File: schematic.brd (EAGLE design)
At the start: 52.1 x 134.6 mm, 101 parts, among them IC1 AD8015, IC2 AD8015, IC3 AD8015, IC4 AD8015

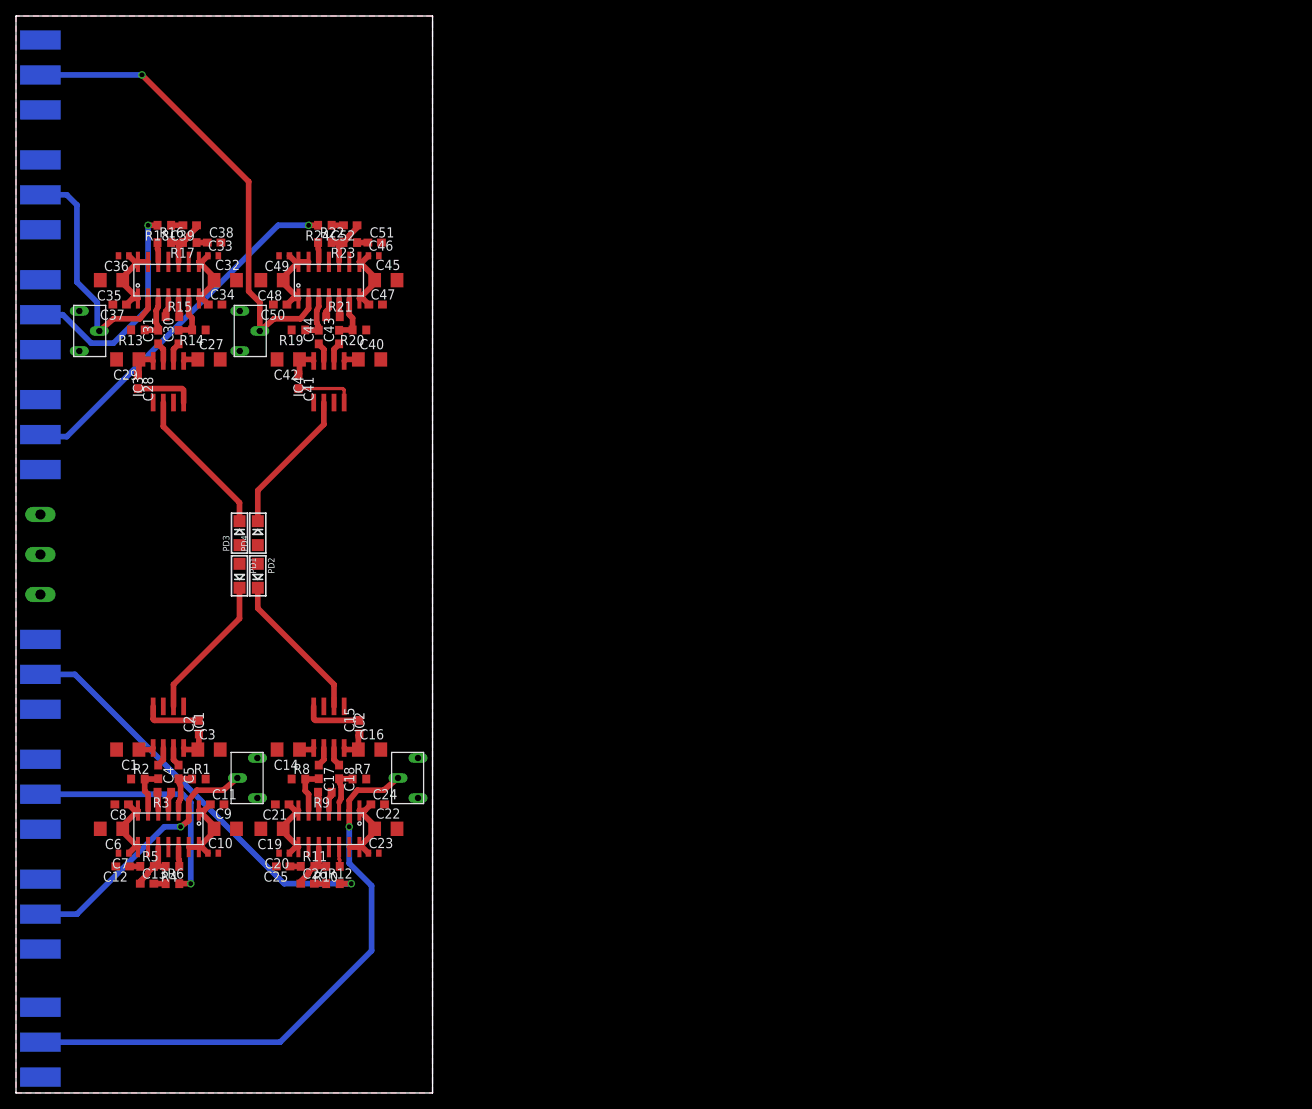
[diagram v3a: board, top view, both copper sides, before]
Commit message: Added LMH6624 to end. Major layout rework for high freq AC .
Still has problems. LMH6624 has power inputs on the wrong side of the
chip making it hard to wire to power plane. GND plane is heavily split
in the process of connecting power planes.
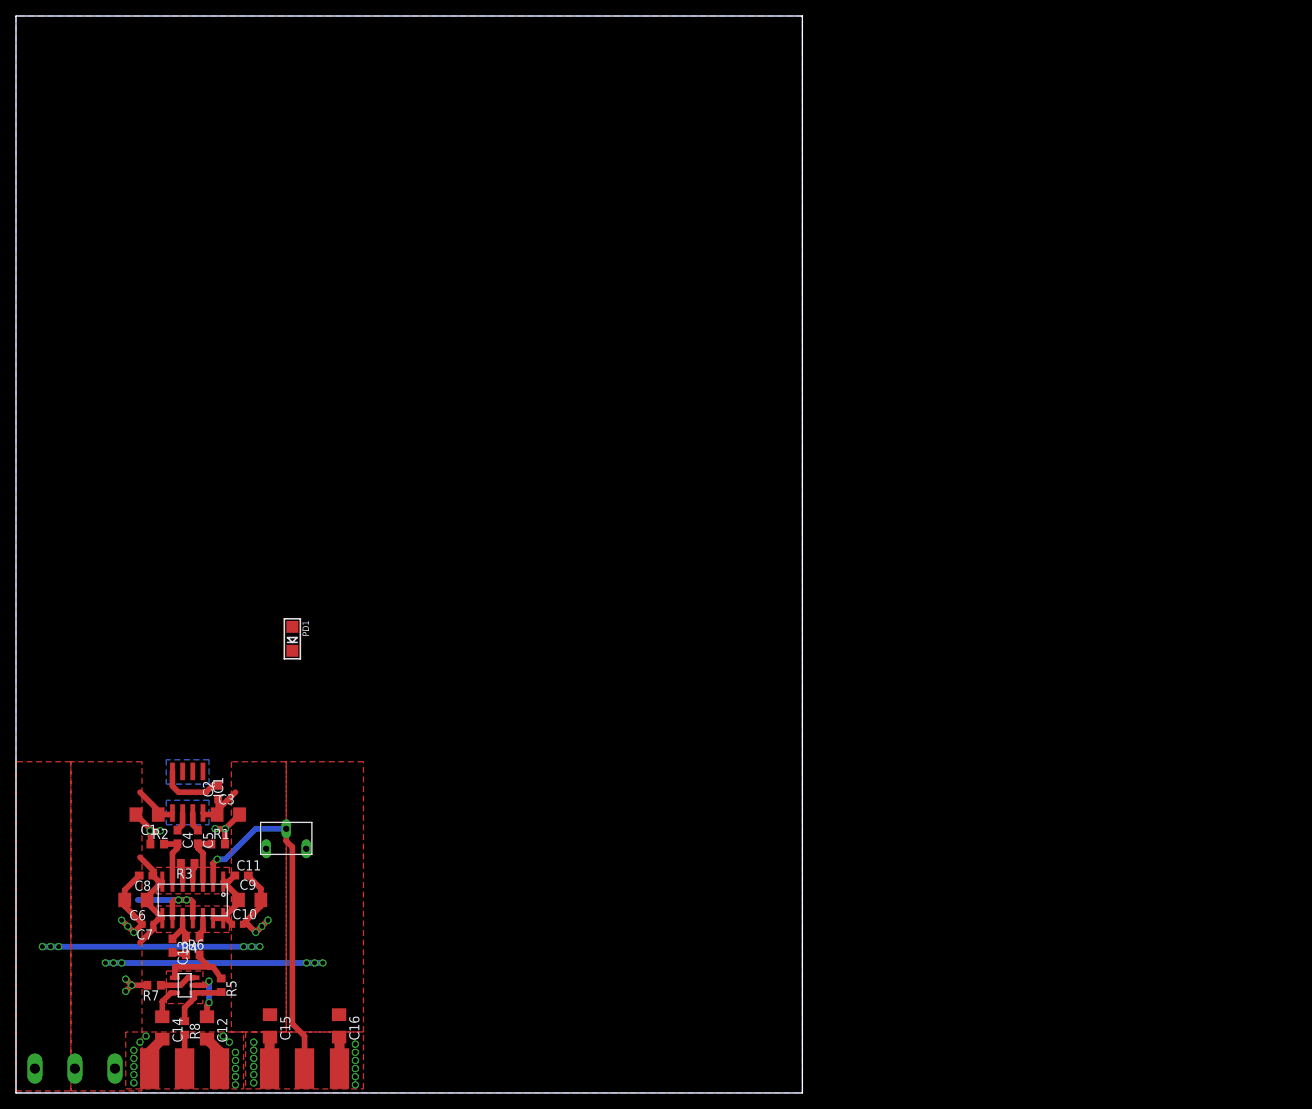
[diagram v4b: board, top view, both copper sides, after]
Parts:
- removed C17, C18, C28, C30, C31, C41, C43, C44: .1uF, rcl:C0603
- removed C19, C22, C27, C29, C32, C35, C40, C42, C45, C48: 6.8uF, rcl:C1206
- removed C20, C23, C33, C36, C46, C49: 0.1uF, rcl:C0402
- removed C21, C24, C26, C34, C37, C39, C47, C50, C52: 0.1uF, rcl:C0603
- removed C25, C38, C51: 39pF, rcl:C0603
- removed IC2, IC3, IC4: AD8015, analog-devices:SO8
- removed PD2, PD3, PD4: (no value), microbuilder:CHIPLED_1206
- removed R10, R16, R22: 1k, rcl:R0603
- removed R11, R12, R15, R17, R18, R21, R23, R24, R9: 100, rcl:R0603
- removed R13, R14, R19, R20: 50, rcl:R0603
- removed U$10, U$14: LMH6503, 12-ChannelEMG:SOIC14
- removed U$11, U$15, U$7: PV37W, 12-ChannelEMG:PV37W
- removed U$12, U$13, U$16, U$17, U$8, U$9: BNCCONN, 12-ChannelEMG:BNCPADS
- C12: value 39pF -> 6.8uF; device rcl:C0603 -> rcl:C1206
- C13: value 0.1uF -> 2.2uF
- C15: value .1uF -> 6.8uF; device rcl:C0603 -> rcl:C1206
- C4, C5: value .1uF -> 2.2uF
- R5: value 100 -> 500
- R6: value 100 -> 30
- R7: value 50 -> 28
- U$6: value LMH6503 -> LMH6624; device 12-ChannelEMG:SOIC14 -> 12-ChannelEMG:SOT-23
- moved U$3 64.4 mm to (7.37, 3.05), turned to 180 degrees
- moved C15 39.0 mm to (31.8, 8.38), turned to 270 degrees
- moved U$5 38.7 mm to (21.1, 3.05), flipped to the top, turned to 0 degrees
- moved U$4 38.2 mm to (36.1, 3.05), flipped to the top, turned to 0 degrees
- moved C14 38.2 mm to (18.3, 8.13), turned to 270 degrees
- moved R7 36.4 mm to (17.3, 13.5), turned to 180 degrees
- moved C16 34.8 mm to (40.4, 8.38), turned to 270 degrees
- moved R8 34.2 mm to (21.1, 8.13), turned to 270 degrees
- moved U$6 26.6 mm to (21.1, 13.5), turned to 90 degrees
- moved C12 22.8 mm to (23.9, 8.13), turned to 270 degrees
- moved R5 17.5 mm to (25.7, 13.5), turned to 270 degrees
- moved PD1 10.3 mm to (34.5, 56.8)
- moved C6 9.40 mm to (15.0, 24.1)
- moved C9 9.40 mm to (29.2, 24.1)
- moved U$1 9.40 mm to (22.1, 24.1)
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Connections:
- removed net N$17: C18.1, IC2.7
- removed net N$18: C17.1, IC2.6
- removed net N$19: C17.2, R8.2, U$6.6
- removed net N$20: C18.2, R7.1, U$6.3
- removed net N$21: R9.1, U$6.4
- removed net N$22: R9.2, U$6.5
- removed net N$23: R10.1, U$6.12
- removed net N$24: C26.1, R10.2, R11.2, U$6.10
- removed net N$25: C25.1, R11.1
- removed net N$26: C26.2, R12.1
- removed net N$27: U$6.2, U$7.2, U$8.2
- removed net N$28: R12.2, U$9.2
- removed net N$29: C28.2, IC3.4
- removed net N$30: IC3.2, PD3.C
- removed net N$31: C31.1, IC3.7
- removed net N$32: C30.1, IC3.6
- removed net N$33: C30.2, R14.2, U$10.6
- removed net N$34: C31.2, R13.1, U$10.3
- removed net N$35: R15.1, U$10.4
- removed net N$36: R15.2, U$10.5
- removed net N$37: R16.1, U$10.12
- removed net N$38: C39.1, R16.2, R17.2, U$10.10
- removed net N$39: C38.1, R17.1
- removed net N$40: C39.2, R18.1
- removed net N$41: U$10.2, U$11.2, U$12.2
- removed net N$42: R18.2, U$13.2
- removed net N$43: C41.2, IC4.4
- removed net N$44: IC4.2, PD4.C
- removed net N$45: C44.1, IC4.7
- removed net N$46: C43.1, IC4.6
- removed net N$47: C43.2, R20.2, U$14.6
- removed net N$48: C44.2, R19.1, U$14.3
- removed net N$49: R21.1, U$14.4
- removed net N$50: R21.2, U$14.5
- removed net N$51: R22.1, U$14.12
- removed net N$52: C52.1, R22.2, R23.2, U$14.10
- removed net N$53: C51.1, R23.1
- removed net N$54: C52.2, R24.1
- removed net N$55: U$14.2, U$15.2, U$16.2
- removed net N$56: R24.2, U$17.2
- net +5V: now also C14.1, U$3.+5V, U$6.5; no longer C16.1, C22.1, C23.1, C24.1, C28.1, C29.1, C35.1, C36.1, C37.1, C41.1, C42.1, C48.1, C49.1, C50.1, IC2.8, IC3.8, IC4.8, U$10.1, U$10.13, U$10.14, U$11.1, U$14.1, U$14.13, U$14.14, U$15.1, U$3.+5, U$6.1, U$6.13, U$6.14, U$7.1
- net -5V: now also C12.1, C16.1, U$6.2; no longer C14.1, C19.1, C20.1, C21.1, C27.1, C32.1, C33.1, C34.1, C40.1, C45.1, C46.1, C47.1, IC2.5, IC3.5, IC4.5, PD2.A, PD3.A, PD4.A, U$10.7, U$10.8, U$11.3, U$14.7, U$14.8, U$15.3, U$6.7, U$6.8, U$7.3
- net GND: now also C15.2; no longer C19.2, C20.2, C21.2, C22.2, C23.2, C24.2, C25.2, C27.2, C29.2, C32.2, C33.2, C34.2, C35.2, C36.2, C37.2, C38.2, C40.2, C42.2, C45.2, C46.2, C47.2, C48.2, C49.2, C50.2, C51.2, R13.2, R14.1, R19.2, R20.1, R8.1, U$10.11, U$10.9, U$12.1, U$12.3, U$13.1, U$13.3, U$14.11, U$14.9, U$16.1, U$16.3, U$17.1, U$17.3, U$6.11, U$6.9, U$8.1, U$8.3, U$9.1, U$9.3
- net N$10: no longer R5.2
- net N$11: now also R6.2, U$6.4; no longer C12.1
- net N$14: now also R8.2; no longer R6.2
- net N$15: now also R7.1, U$6.3; no longer C15.2, IC2.4
- net N$16: now also R5.2, R8.1, U$6.1; no longer IC2.2, PD2.C
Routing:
- net N$27: track 73.4 -> 0.00 mm, vias 1 -> 0
- net GND: track 0.00 -> 69.2 mm, vias 0 -> 41
- net N$55: track 59.3 -> 0.00 mm, vias 1 -> 0
- net N$28: track 51.1 -> 0.00 mm, vias 1 -> 0
- net N$56: track 45.8 -> 0.00 mm, vias 1 -> 0
- net N$41: track 30.5 -> 0.00 mm
- net N$42: track 28.3 -> 0.00 mm, vias 1 -> 0
- net N$14: track 32.5 -> 4.23 mm, vias 1 -> 0
- net N$30: track 18.8 -> 0.00 mm
- net N$44: track 18.2 -> 0.00 mm
- net N$1: track 18.2 -> 0.00 mm
- net N$16: track 18.8 -> 7.43 mm
- net N$13: track 33.1 -> 44.1 mm
- net -5V: track 43.8 -> 54.4 mm, vias 0 -> 8
- net +5V: track 57.9 -> 49.1 mm, vias 0 -> 6
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- added copper zone on layer 1, net +5V
- added copper zone on layer 1, net -5V
- added copper zone on layer 1, net N$18
- added copper zone on layer 16, net N$18
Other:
- board size 52.1 x 134.6 mm -> 98.3 x 134.6 mm
- board text added: "+5V"
- board text added: "-5V"

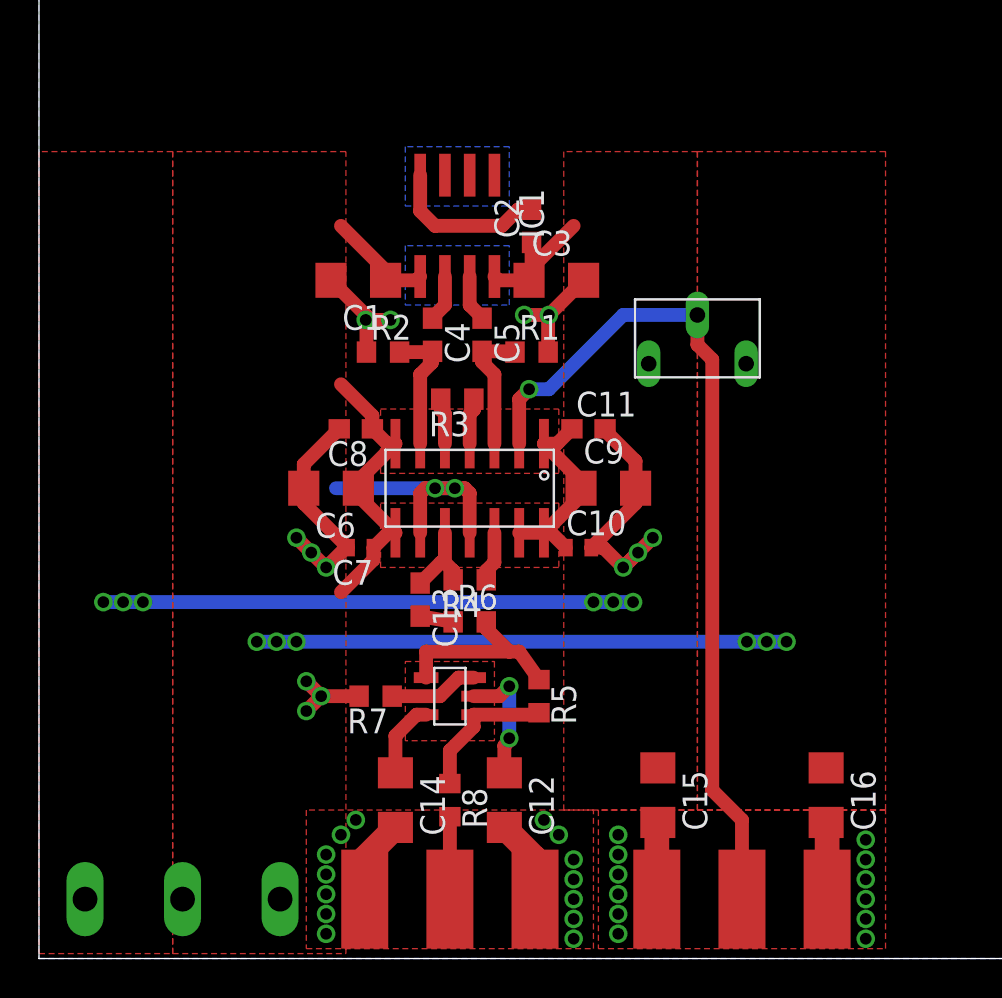
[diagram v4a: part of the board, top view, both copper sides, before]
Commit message: Updated LMH6624 Layout to be able to reach power with minimal capacitance on the feedback loop
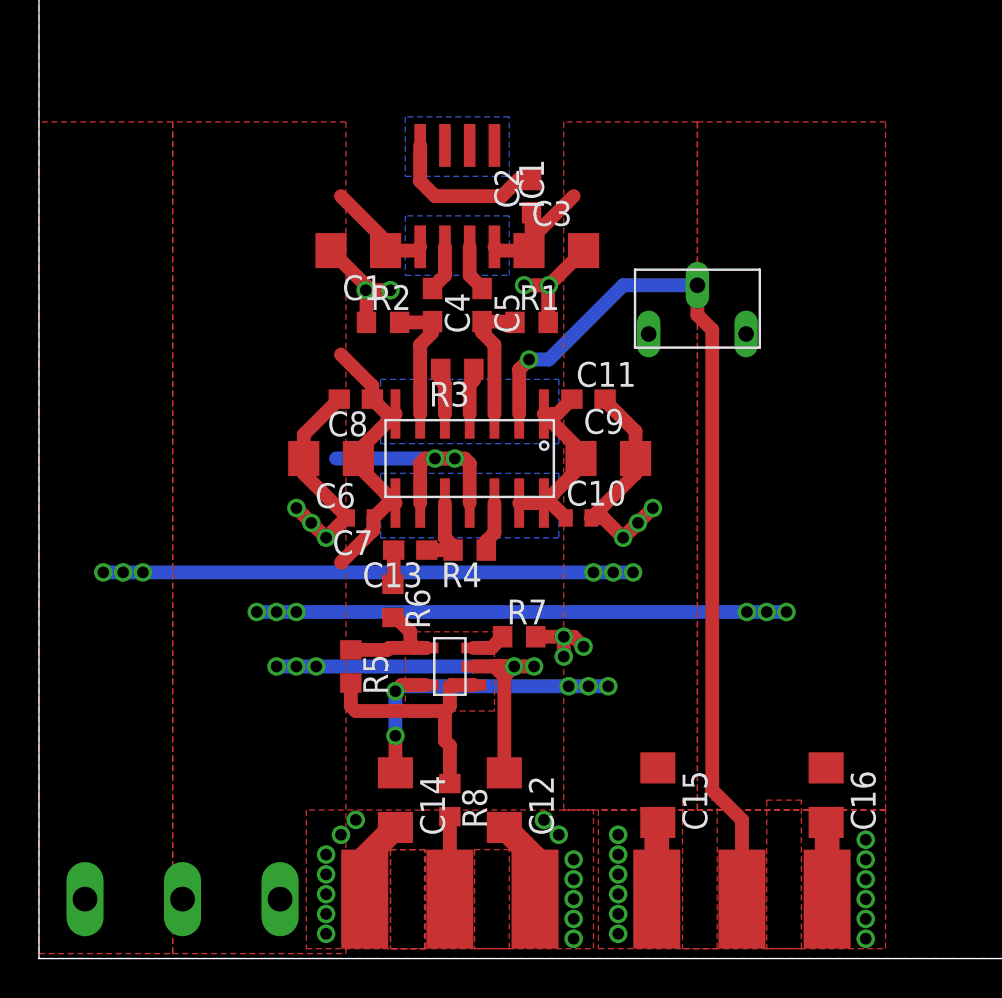
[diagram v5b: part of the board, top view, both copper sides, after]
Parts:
- moved R5 9.77 mm to (16.0, 15.0)
- moved R7 7.97 mm to (24.6, 16.5), turned to 0 degrees
- moved R6 4.08 mm to (18.2, 18.4), turned to 270 degrees
- moved C13 2.59 mm to (19.1, 21.0), turned to 180 degrees
- moved R1 1.52 mm to (25.3, 32.6)
- moved R2 1.52 mm to (17.7, 32.6)
- moved C1 1.52 mm to (16.4, 36.3)
- moved C10 1.52 mm to (27.7, 22.6)
- moved C11 1.52 mm to (28.2, 28.7)
- moved C2 1.52 mm to (25.3, 39.1)
- moved C3 1.52 mm to (26.5, 36.3)
- moved C4 1.52 mm to (20.2, 33.5)
- moved C5 1.52 mm to (22.7, 33.5)
- moved C6 1.52 mm to (15.0, 25.7)
- moved C7 1.52 mm to (16.5, 22.6)
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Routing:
- net -5V: track 54.4 -> 71.5 mm, vias 8 -> 11
- net +5V: track 49.1 -> 62.1 mm, vias 6 -> 11
- net N$16: track 7.43 -> 12.6 mm
- net N$11: track 9.88 -> 6.03 mm
- net N$15: track 4.57 -> 1.72 mm
- net N$13: track 44.1 -> 45.7 mm
- added copper zone on layer 1, net N$19
- added copper zone on layer 1, net N$20
- added copper zone on layer 1, net N$21
- added copper zone on layer 1, net N$22
- added copper zone on layer 1, net N$23

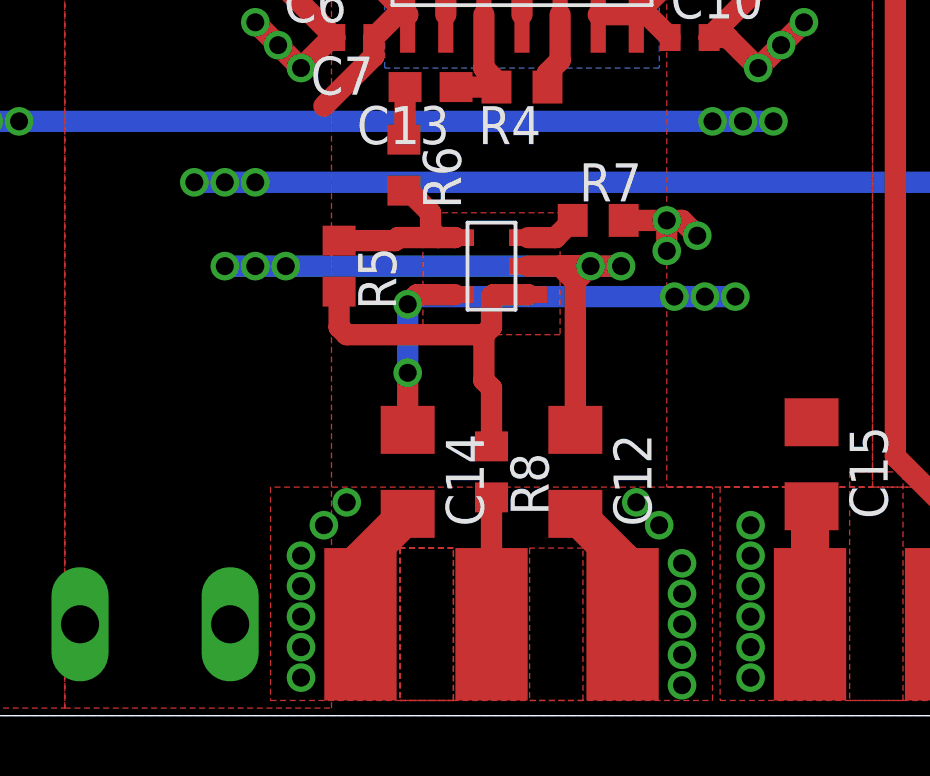
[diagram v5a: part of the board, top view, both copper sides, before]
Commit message: Removed some congestion by the LMH6624
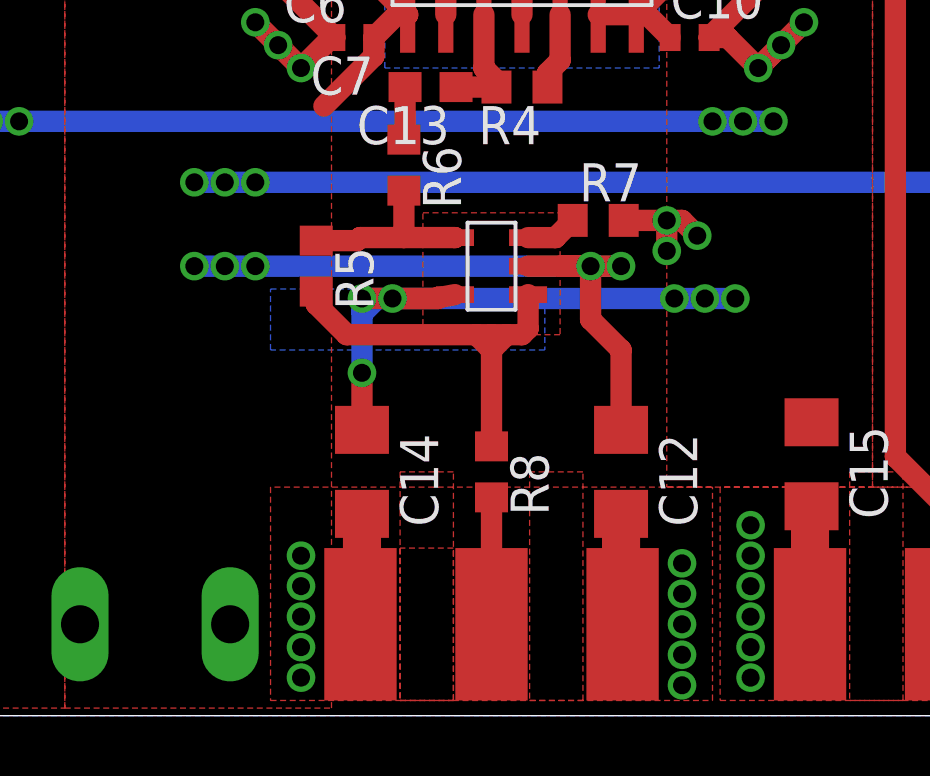
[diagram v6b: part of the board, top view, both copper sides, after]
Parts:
- moved C14 1.52 mm to (16.8, 8.13)
- moved C12 1.52 mm to (25.4, 8.13)
- moved R5 0.76 mm to (15.2, 15.0)
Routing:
- net +5V: track 62.1 -> 67.5 mm, vias 11 -> 12
- net N$16: track 12.6 -> 14.3 mm
- net -5V: track 71.5 -> 72.0 mm
- net GND: track 69.1 -> 69.0 mm, vias 41 -> 37
- added copper zone on layer 16, net N$20
